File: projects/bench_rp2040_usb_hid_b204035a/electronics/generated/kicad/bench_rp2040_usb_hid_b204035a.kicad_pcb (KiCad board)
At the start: 2 copper layers, 51 x 21 mm, 10 parts, among them J1 USB-C POWER, J2 SWD 10-pin, U1 3V3 LDO, U2 RP2040, U3 2MB QSPI, X1 12MHz XTAL

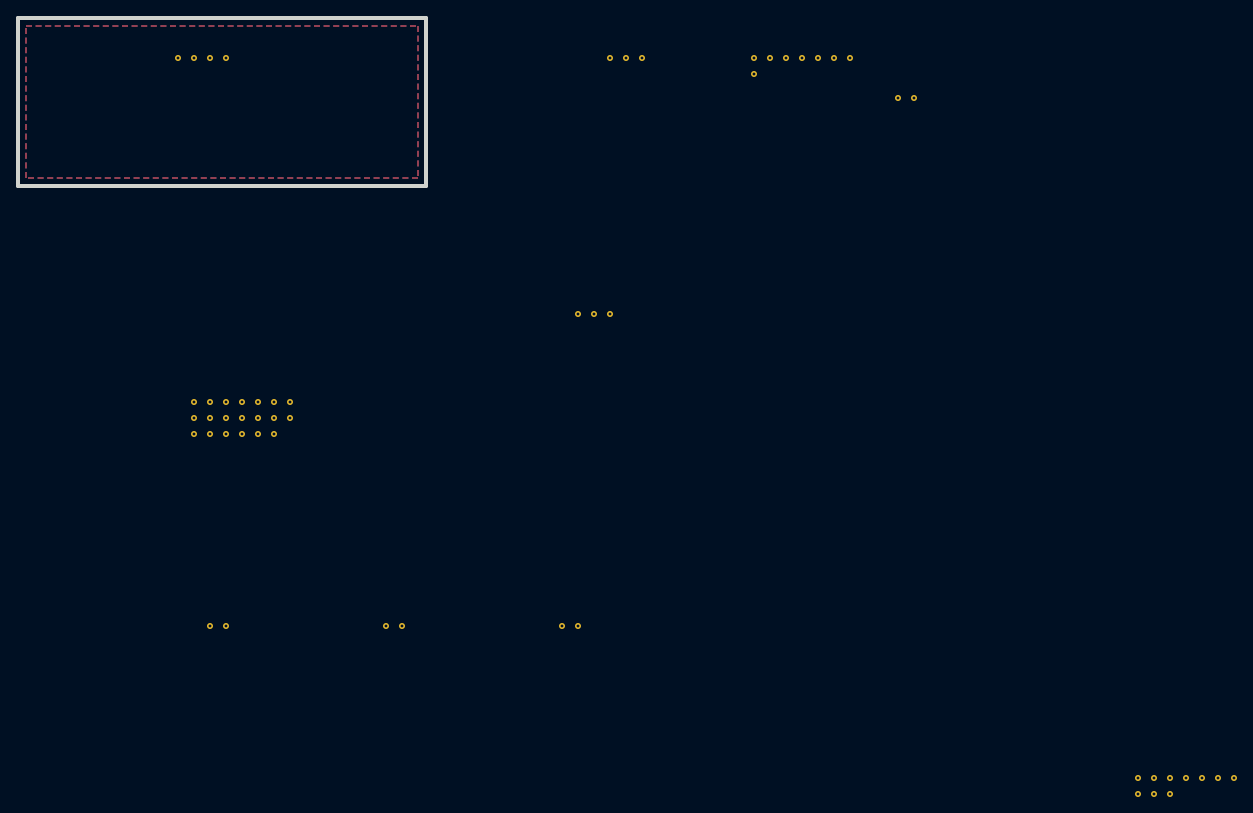
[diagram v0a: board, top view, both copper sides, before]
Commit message: chore: refresh rp2040 benchmark evidence
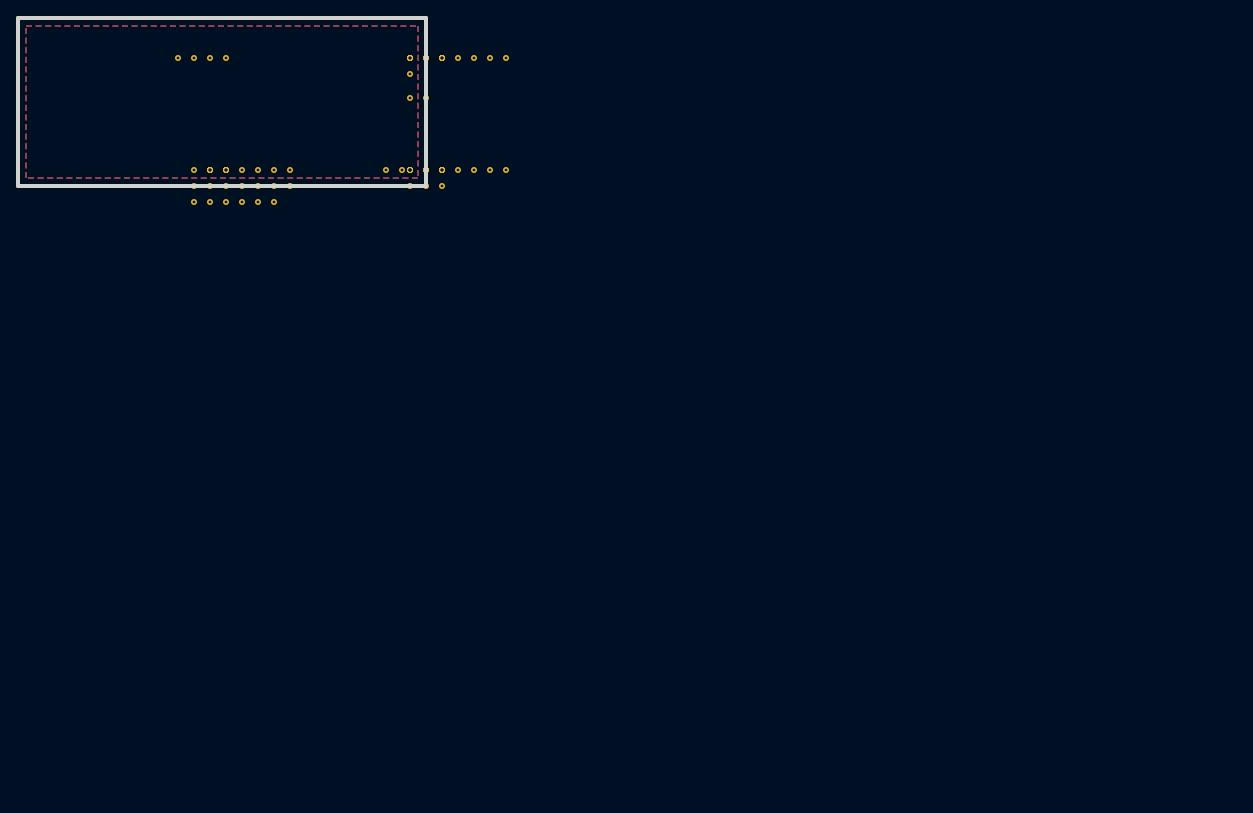
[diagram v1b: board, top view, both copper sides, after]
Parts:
- moved J2 118.6 mm to (49.0, 19.0)
- moved X1 61.0 mm to (49.0, 10.0)
- moved C3 60.1 mm to (49.0, 19.0)
- moved C1 57.0 mm to (24.0, 19.0)
- moved C2 57.0 mm to (46.0, 19.0)
- moved U3 43.0 mm to (49.0, 5.00)
- moved U2 29.0 mm to (22.0, 19.0)
- moved U1 27.7 mm to (49.0, 19.0)
- moved D1 25.0 mm to (49.0, 5.00)
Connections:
- U3 pad 3: V3V3 -> QSPI_D2
- U3 pad 7: V3V3 -> QSPI_D3
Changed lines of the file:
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@@
     (pad "3" thru_hole circle (at 4.000 0.000) (size 0.75 0.75) (drill 0.35) (layers "*.Cu" "*.Mask") (net 10 "USB_DM"))
     (pad "4" thru_hole circle (at 6.000 0.000) (size 0.75 0.75) (drill 0.35) (layers "*.Cu" "*.Mask") (net 1 "GND")))
-  (footprint "Package_TO_SOT_SMD:SOT-23-6" (layer "F.Cu") (at 74.0 5.0)
+  (footprint "Package_TO_SOT_SMD:SOT-23-6" (layer "F.Cu") (at 49.0 5.0)
     (property "Reference" "D1" (at 0 -3 0) (layer "F.Fab"))
     (property "Value" "USB ESD" (at 0 3 0) (layer "F.Fab"))
@@
     (pad "2" thru_hole circle (at 2.000 0.000) (size 0.75 0.75) (drill 0.35) (layers "*.Cu" "*.Mask") (net 1 "GND"))
     (pad "3" thru_hole circle (at 4.000 0.000) (size 0.75 0.75) (drill 0.35) (layers "*.Cu" "*.Mask") (net 10 "USB_DM")))
-  (footprint "Package_TO_SOT_SMD:SOT-23-5" (layer "F.Cu") (at 70.0 37.0)
+  (footprint "Package_TO_SOT_SMD:SOT-23-5" (layer "F.Cu") (at 49.0 19.0)
     (property "Reference" "U1" (at 0 -3 0) (layer "F.Fab"))
     (property "Value" "3V3 LDO" (at 0 3 0) (layer "F.Fab"))
@@
     (pad "2" thru_hole circle (at 2.000 0.000) (size 0.75 0.75) (drill 0.35) (layers "*.Cu" "*.Mask") (net 1 "GND"))
     (pad "3" thru_hole circle (at 4.000 0.000) (size 0.75 0.75) (drill 0.35) (layers "*.Cu" "*.Mask") (net 13 "V3V3")))
-  (footprint "Package_DFN_QFN:QFN-56-1EP_7x7mm_P0.4mm_EP3.2x3.2mm" (layer "F.Cu") (at 22.0 48.0)
+  (footprint "Package_DFN_QFN:QFN-56-1EP_7x7mm_P0.4mm_EP3.2x3.2mm" (layer "F.Cu") (at 22.0 19.0)
     (property "Reference" "U2" (at 0 -3 0) (layer "F.Fab"))
     (property "Value" "RP2040" (at 0 3 0) (layer "F.Fab"))
@@
     (pad "47" thru_hole circle (at 8.000 4.000) (size 0.75 0.75) (drill 0.35) (layers "*.Cu" "*.Mask") (net 13 "V3V3"))
     (pad "48" thru_hole circle (at 10.000 4.000) (size 0.75 0.75) (drill 0.35) (layers "*.Cu" "*.Mask") (net 13 "V3V3")))
-  (footprint "Package_SO:SOIC-8_3.9x4.9mm_P1.27mm" (layer "F.Cu") (at 92.0 5.0)
+  (footprint "Package_SO:SOIC-8_3.9x4.9mm_P1.27mm" (layer "F.Cu") (at 49.0 5.0)
     (property "Reference" "U3" (at 0 -3 0) (layer "F.Fab"))
     (property "Value" "2MB QSPI" (at 0 3 0) (layer "F.Fab"))
@@
     (pad "1" thru_hole circle (at 0.000 0.000) (size 0.75 0.75) (drill 0.35) (layers "*.Cu" "*.Mask") (net 3 "QSPI_CS"))
     (pad "2" thru_hole circle (at 2.000 0.000) (size 0.75 0.75) (drill 0.35) (layers "*.Cu" "*.Mask") (net 6 "QSPI_MISO"))
-    (pad "3" thru_hole circle (at 4.000 0.000) (size 0.75 0.75) (drill 0.35) (layers "*.Cu" "*.Mask") (net 13 "V3V3"))
+    (pad "3" thru_hole circle (at 4.000 0.000) (size 0.75 0.75) (drill 0.35) (layers "*.Cu" "*.Mask") (net 4 "QSPI_D2"))
     (pad "4" thru_hole circle (at 6.000 0.000) (size 0.75 0.75) (drill 0.35) (layers "*.Cu" "*.Mask") (net 1 "GND"))
     (pad "5" thru_hole circle (at 8.000 0.000) (size 0.75 0.75) (drill 0.35) (layers "*.Cu" "*.Mask") (net 7 "QSPI_MOSI"))
     (pad "6" thru_hole circle (at 10.000 0.000) (size 0.75 0.75) (drill 0.35) (layers "*.Cu" "*.Mask") (net 2 "QSPI_CLK"))
-    (pad "7" thru_hole circle (at 12.000 0.000) (size 0.75 0.75) (drill 0.35) (layers "*.Cu" "*.Mask") (net 13 "V3V3"))
+    (pad "7" thru_hole circle (at 12.000 0.000) (size 0.75 0.75) (drill 0.35) (layers "*.Cu" "*.Mask") (net 5 "QSPI_D3"))
     (pad "8" thru_hole circle (at 0.000 2.000) (size 0.75 0.75) (drill 0.35) (layers "*.Cu" "*.Mask") (net 13 "V3V3")))
-  (footprint "Crystal:Crystal_SMD_HC-49S" (layer "F.Cu") (at 110.0 10.0)
+  (footprint "Crystal:Crystal_SMD_HC-49S" (layer "F.Cu") (at 49.0 10.0)
     (property "Reference" "X1" (at 0 -3 0) (layer "F.Fab"))
     (property "Value" "12MHz XTAL" (at 0 3 0) (layer "F.Fab"))
@@
     (pad "1" thru_hole circle (at 0.000 0.000) (size 0.75 0.75) (drill 0.35) (layers "*.Cu" "*.Mask") (net 14 "XIN"))
     (pad "2" thru_hole circle (at 2.000 0.000) (size 0.75 0.75) (drill 0.35) (layers "*.Cu" "*.Mask") (net 15 "XOUT")))
-  (footprint "Connector_PinHeader_2.54mm:PinHeader_2x05_P2.54mm_Vertical" (layer "F.Cu") (at 140.0 95.0)
+  (footprint "Connector_PinHeader_2.54mm:PinHeader_2x05_P2.54mm_Vertical" (layer "F.Cu") (at 49.0 19.0)
     (property "Reference" "J2" (at 0 -3 0) (layer "F.Fab"))
     (property "Value" "SWD 10-pin" (at 0 3 0) (layer "F.Fab"))
@@
     (pad "9" thru_hole circle (at 2.000 2.000) (size 0.75 0.75) (drill 0.35) (layers "*.Cu" "*.Mask") (net 1 "GND"))
     (pad "10" thru_hole circle (at 4.000 2.000) (size 0.75 0.75) (drill 0.35) (layers "*.Cu" "*.Mask") (net 1 "GND")))
-  (footprint "Capacitor_SMD:C_0402_1005Metric" (layer "F.Cu") (at 24.0 76.0)
+  (footprint "Capacitor_SMD:C_0402_1005Metric" (layer "F.Cu") (at 24.0 19.0)
     (property "Reference" "C1" (at 0 -3 0) (layer "F.Fab"))
     (property "Value" "100nF" (at 0 3 0) (layer "F.Fab"))
@@
     (pad "1" thru_hole circle (at 0.000 0.000) (size 0.75 0.75) (drill 0.35) (layers "*.Cu" "*.Mask") (net 13 "V3V3"))
     (pad "2" thru_hole circle (at 2.000 0.000) (size 0.75 0.75) (drill 0.35) (layers "*.Cu" "*.Mask") (net 1 "GND")))
-  (footprint "Capacitor_SMD:C_0402_1005Metric" (layer "F.Cu") (at 46.0 76.0)
+  (footprint "Capacitor_SMD:C_0402_1005Metric" (layer "F.Cu") (at 46.0 19.0)
     (property "Reference" "C2" (at 0 -3 0) (layer "F.Fab"))
     (property "Value" "100nF" (at 0 3 0) (layer "F.Fab"))
@@
     (pad "1" thru_hole circle (at 0.000 0.000) (size 0.75 0.75) (drill 0.35) (layers "*.Cu" "*.Mask") (net 13 "V3V3"))
     (pad "2" thru_hole circle (at 2.000 0.000) (size 0.75 0.75) (drill 0.35) (layers "*.Cu" "*.Mask") (net 1 "GND")))
-  (footprint "Capacitor_SMD:C_0603_1608Metric" (layer "F.Cu") (at 68.0 76.0)
+  (footprint "Capacitor_SMD:C_0603_1608Metric" (layer "F.Cu") (at 49.0 19.0)
     (property "Reference" "C3" (at 0 -3 0) (layer "F.Fab"))
     (property "Value" "10uF" (at 0 3 0) (layer "F.Fab"))

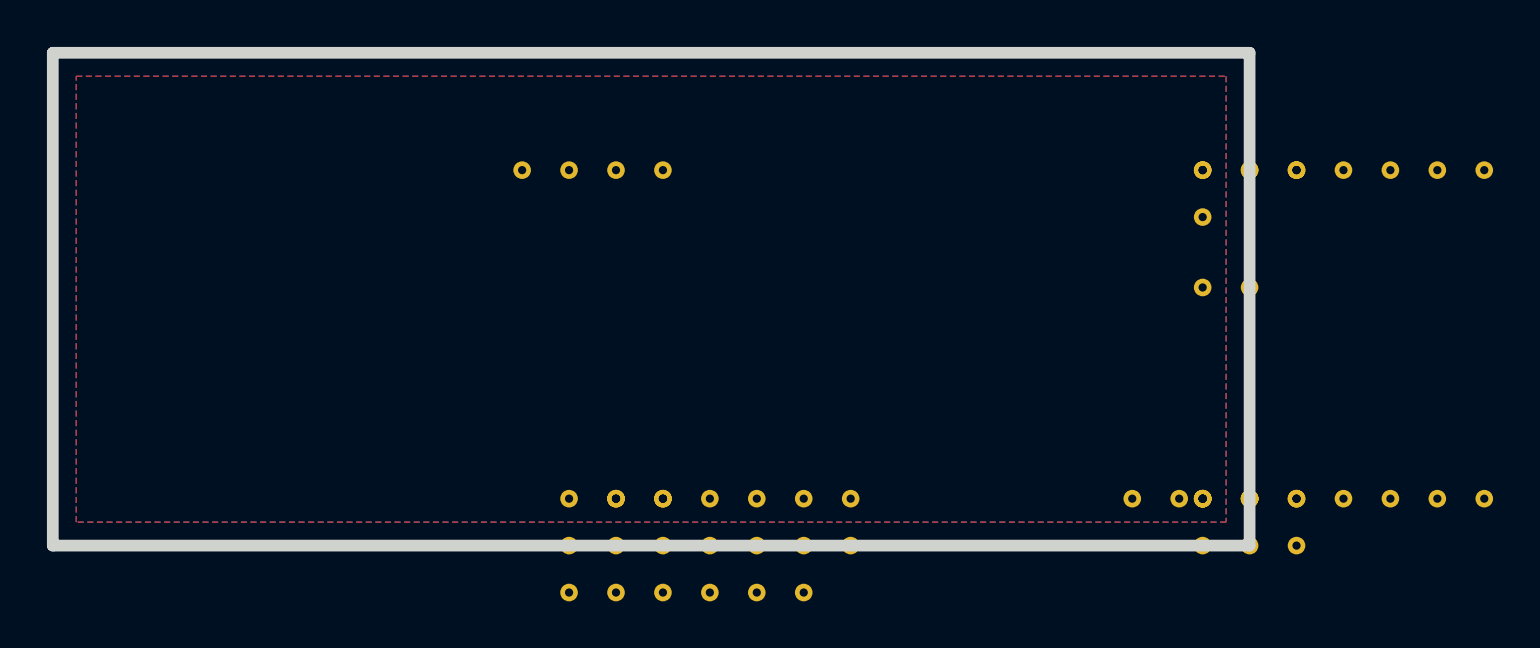
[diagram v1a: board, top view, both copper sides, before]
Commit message: feat: ground rp2040 placement evidence
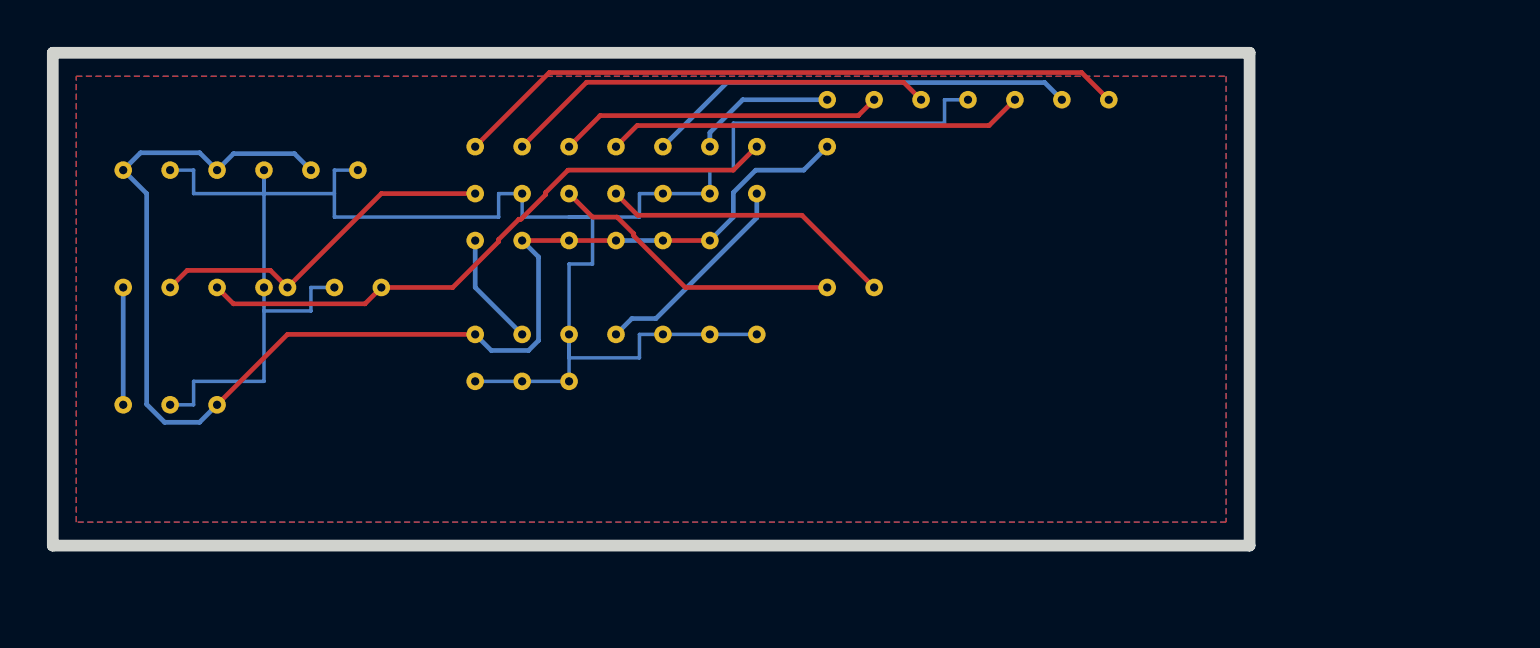
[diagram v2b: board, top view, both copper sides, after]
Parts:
- moved U1 46.2 mm to (3.00, 15.0)
- moved C2 41.4 mm to (7.00, 5.00)
- moved C3 40.5 mm to (11.0, 5.00)
- moved D1 39.3 mm to (10.0, 10.0)
- moved J2 31.8 mm to (18.0, 12.0)
- moved C1 25.2 mm to (3.00, 5.00)
- moved J1 17.7 mm to (3.00, 10.0)
- moved U3 16.3 mm to (33.0, 2.00)
- moved X1 16.0 mm to (33.0, 10.0)
- moved U2 15.5 mm to (18.0, 4.00)
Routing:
- net GND: track 0.00 -> 88.0 mm
- net V3V3: track 0.00 -> 58.4 mm
- net QSPI_D3: track 0.00 -> 28.8 mm
- net USB_DM: track 0.00 -> 26.2 mm
- net QSPI_D2: track 0.00 -> 18.4 mm
- net QSPI_CLK: track 0.00 -> 18.4 mm
- net QSPI_MOSI: track 0.00 -> 17.8 mm
- net USB_DP: track 0.00 -> 15.3 mm
- net QSPI_MISO: track 0.00 -> 13.8 mm
- net XIN: track 0.00 -> 12.7 mm
- net XOUT: track 0.00 -> 12.7 mm
- net SWCLK: track 0.00 -> 9.09 mm
- net QSPI_CS: track 0.00 -> 6.18 mm
- net USB_VBUS: track 0.00 -> 5.00 mm
- net SWDIO: track 0.00 -> 4.83 mm

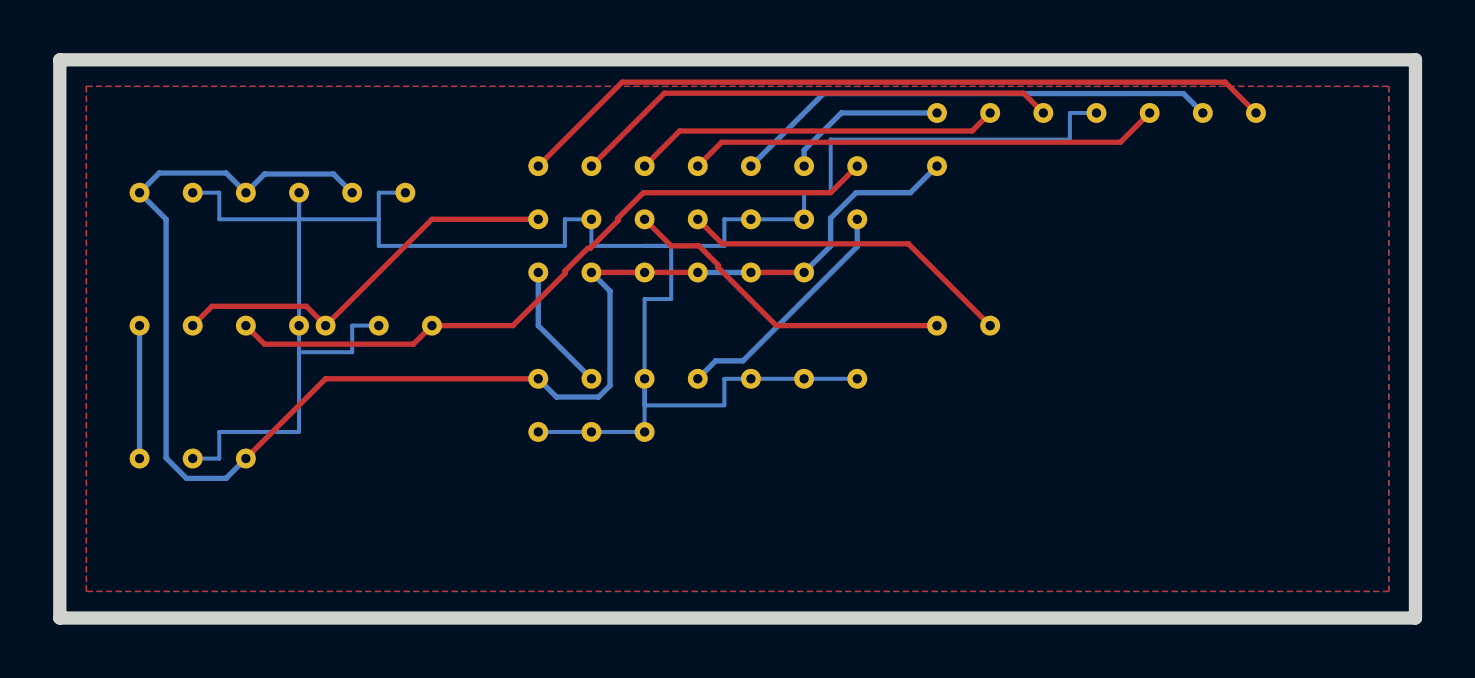
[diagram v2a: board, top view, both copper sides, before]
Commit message: fix: complete rp2040 package pin contract
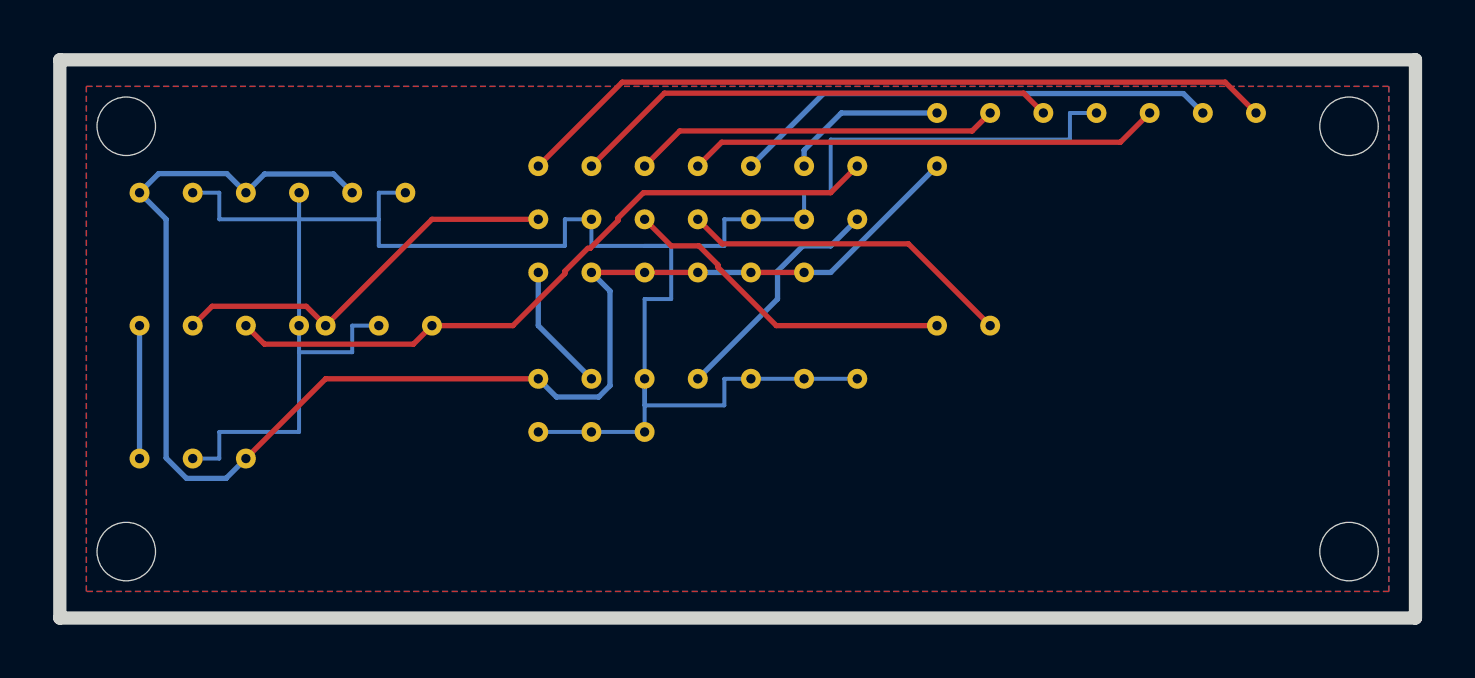
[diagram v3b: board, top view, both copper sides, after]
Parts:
- added H1: MountingHole, MountingHole:MountingHole_2.2mm_Pad, F.Cu at (2.50, 2.50)
- added H2: MountingHole, MountingHole:MountingHole_2.2mm_Pad, F.Cu at (48.5, 2.50)
- added H3: MountingHole, MountingHole:MountingHole_2.2mm_Pad, F.Cu at (2.50, 18.5)
- added H4: MountingHole, MountingHole:MountingHole_2.2mm_Pad, F.Cu at (48.5, 18.5)
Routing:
- net V3V3: track 58.4 -> 57.8 mm
